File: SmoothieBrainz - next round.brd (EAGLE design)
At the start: 101 x 101 mm, 233 parts, among them IC1 LPC1769, IC5 LD117ADT33TR, IC7 74LVC1G04, Q1 BSL207SP, Q2 12MHz, SW1 SW_TACT_4P_B, SW3 SW_TACT_4P_B, T1 BC817, U3 USD-SOCKETUSD, X1 MSTBA2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

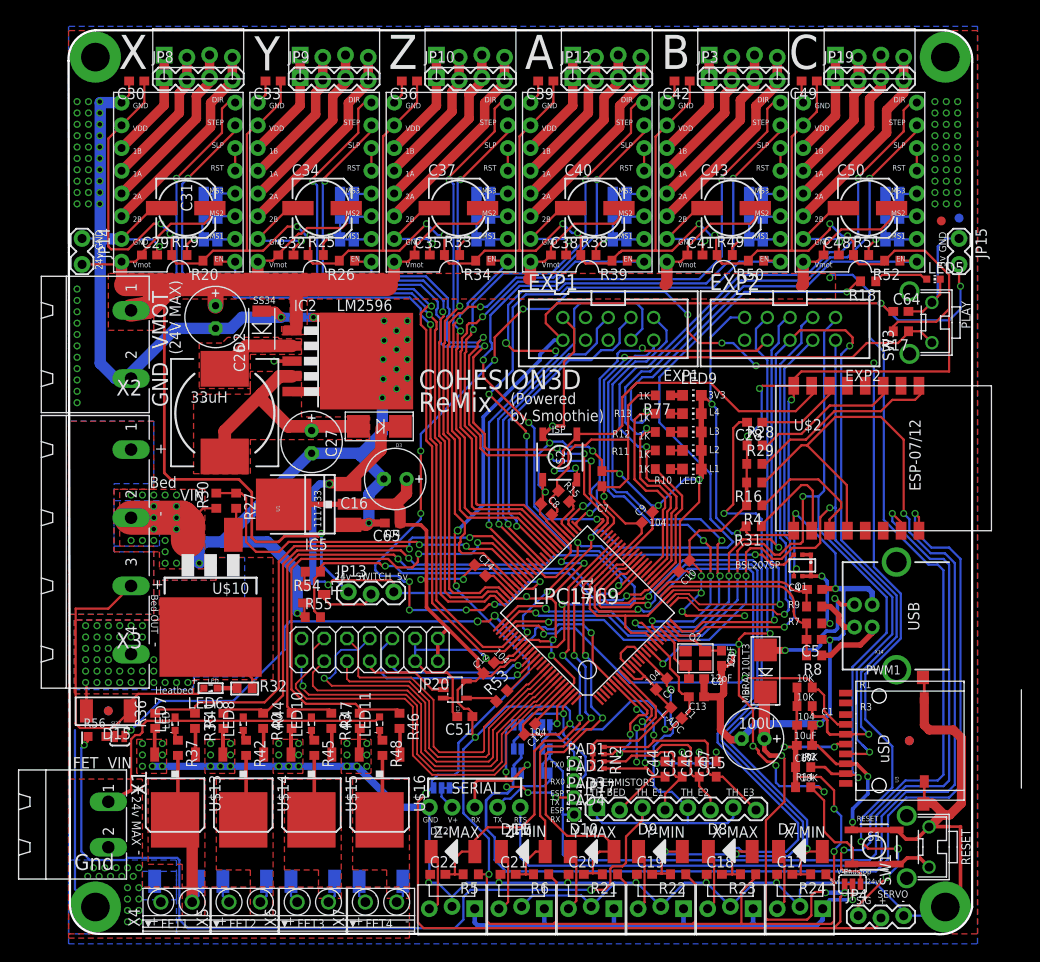
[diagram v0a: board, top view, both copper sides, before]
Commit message: More cleanup.  Changed 100u PTH to SMD
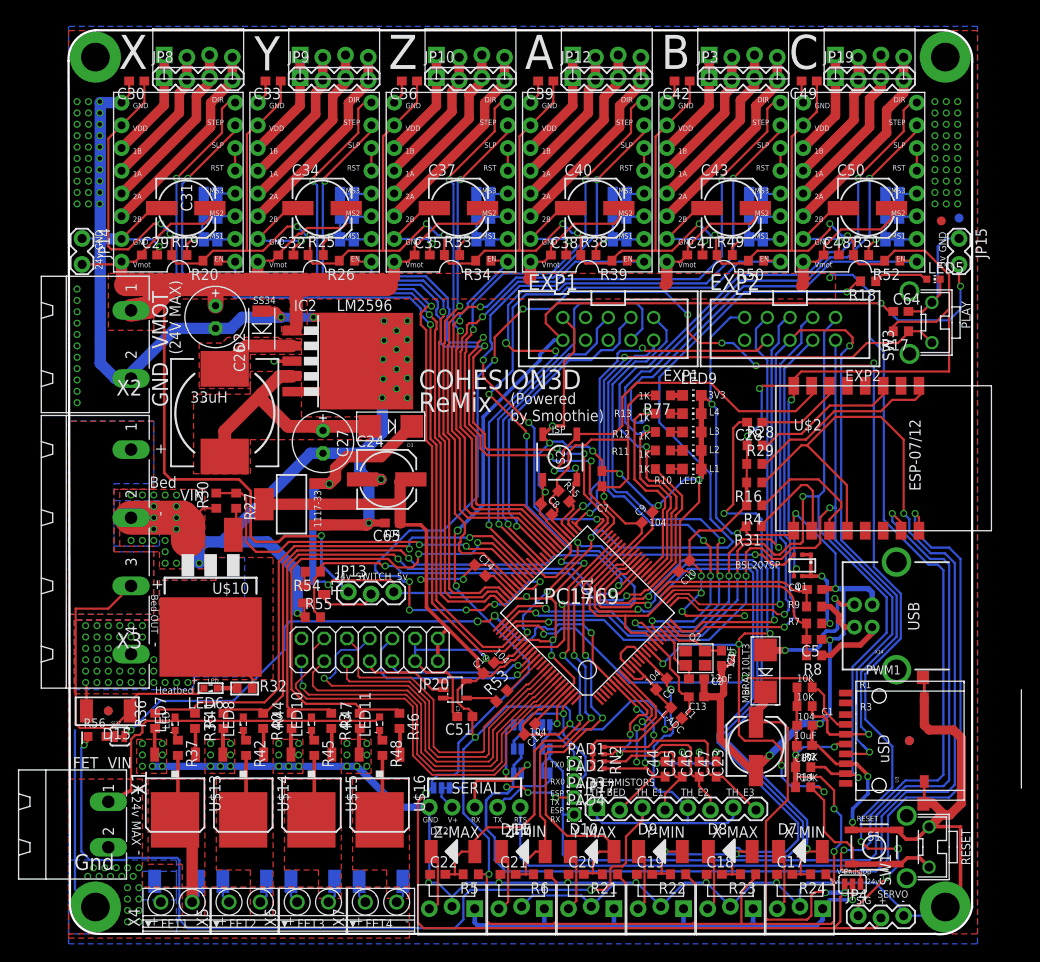
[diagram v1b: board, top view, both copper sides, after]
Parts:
- removed C15: (no value), rcl:E2,5-7
- removed C16: 100U, rcl:E2,5-7
- removed IC5: LD117ADT33TR, v-reg:DPACK
- added C23, C24: 100u, resistor:153CLV-0605
- moved U1 3.18 mm to (24.9, 48.0)
- moved D3 1.27 mm to (36.0, 56.7)
- moved C27 1.27 mm to (28.4, 55.0)
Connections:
- net 3.3V: now also C24.+; no longer C16.+, IC5.4
- net 5V: now also C23.+; no longer C15.+, IC5.3
- net GND: now also C23.-, C24.-; no longer C15.-, C16.-, IC5.1
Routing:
- net GND: track 790.1 -> 799.5 mm, vias 177 -> 179
- net 3.3V: track 696.5 -> 691.8 mm
- net 5V: track 280.0 -> 283.6 mm, vias 10 -> 9
- net PWM0_PSU_OUT: track 181.5 -> 183.7 mm, vias 16 -> 14
- net 5VREG: track 26.2 -> 27.8 mm
- net RESET: track 91.6 -> 92.0 mm, vias 7 -> 6
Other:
- board text removed: "100U"
